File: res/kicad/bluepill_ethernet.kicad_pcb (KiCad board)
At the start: 2 copper layers, 22 parts, among them J1 HEADER-1x20, J2 Conn_01x03, SW1 SW_Push, U1 BluePill_STM32F103C, U2 93C46, U3 WIZ850io

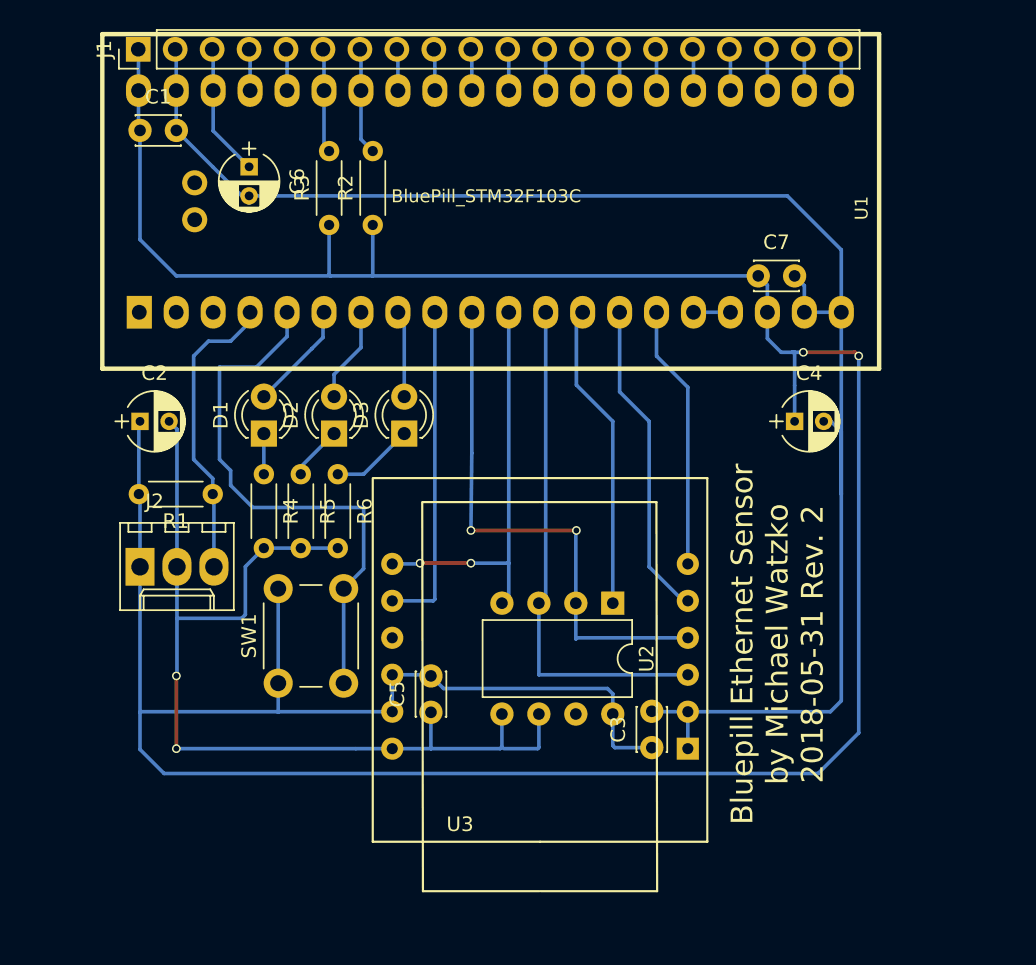
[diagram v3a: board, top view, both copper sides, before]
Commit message: Fix production issues (also add molex pin for other W5500 boards)
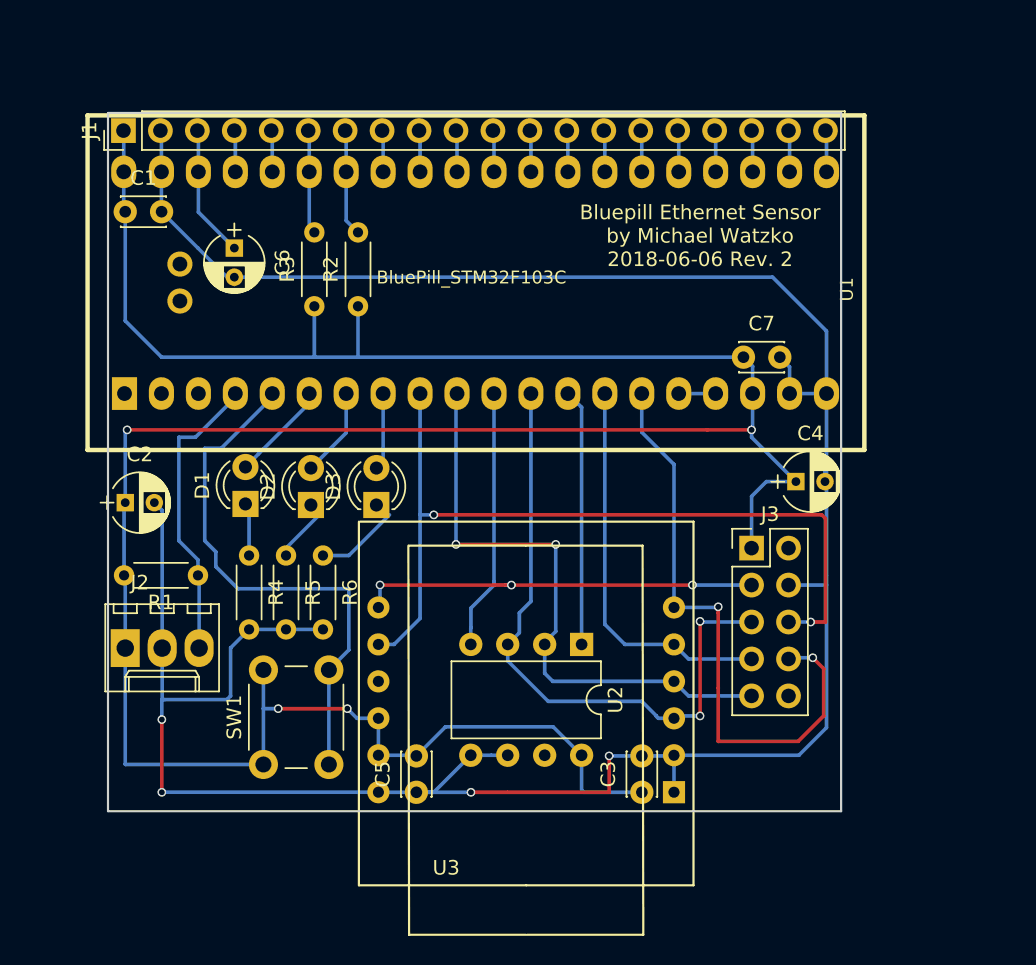
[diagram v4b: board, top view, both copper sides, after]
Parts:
- added J3: Conn_02x05_Odd_Even, Pin_Headers:Pin_Header_Straight_2x05_Pitch2.54mm, F.Cu at (82.0, 61.2)
- moved C7 5.68 mm to (81.5, 48.1)
- moved R4 5.68 mm to (47.5, 61.7)
- moved R5 5.68 mm to (50.0, 61.7)
- moved C1 5.68 mm to (39.0, 38.1)
- moved C2 5.68 mm to (39.0, 58.1)
- moved C6 5.68 mm to (46.5, 40.6)
- moved J1 5.68 mm to (38.9, 32.5)
- moved R1 5.68 mm to (44.0, 63.1)
- moved R2 5.68 mm to (55.0, 44.6)
- moved R3 5.68 mm to (52.0, 44.6)
- moved R6 5.68 mm to (52.6, 61.7)
- moved U1 5.68 mm to (39.0, 50.6)
- moved J2 5.68 mm to (39.0, 68.1)
- moved SW1 5.68 mm to (48.5, 76.1)
- moved C5 5.59 mm to (59.0, 78.0)
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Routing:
- net VCC: track 230.4 -> 195.8 mm, vias 2 -> 4
- net Net-(J3-Pad6): track 22.7 -> 56.7 mm, vias 0 -> 2
- net Net-(J3-Pad8): track 18.2 -> 41.9 mm, vias 0 -> 2
- net Net-(J3-Pad3): track 28.4 -> 46.2 mm, vias 2 -> 3
- net Net-(J3-Pad5): track 35.4 -> 44.0 mm, vias 0 -> 2
- net Net-(J3-Pad7): track 22.0 -> 26.9 mm
- net Net-(J3-Pad9): track 37.5 -> 41.2 mm
- net Net-(U1-Pad13): track 21.2 -> 17.6 mm
- net GND: track 183.1 -> 185.5 mm, vias 2 -> 4
- net Net-(SW1-Pad2): track 38.0 -> 37.2 mm
- net Net-(D3-Pad2): track 5.98 -> 5.31 mm
- net Net-(D1-Pad2): track 7.51 -> 6.87 mm
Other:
- board outline added: 50.4 x 48 mm
- board text added: "Bluepill Ethernet Sensor by Michael Watzko 2018-06-06 Rev. 2"
- board text removed: "Bluepill Ethernet Sensor by Michael Watzko 2018-05-31 Rev. 2"

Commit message: board revision 3 alpha 1
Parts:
- removed C3: C, Capacitors_THT:C_Disc_D3.0mm_W2.0mm_P2.50mm
- added J4: HEADER-1x20, Pin_Headers:Pin_Header_Straight_1x20_Pitch2.54mm, F.Cu at (43.9, 78.2)
- added U4: 93C46, Housings_SSOP:TSSOP-8_4.4x3mm_Pitch0.65mm, F.Cu at (78.9, 41.4)
- C1, C5, C7: footprint Capacitors_THT:C_Disc_D3.0mm_W2.0mm_P2.50mm -> Capacitors_THT:C_Disc_D4.3mm_W1.9mm_P5.00mm
- R1, R2, R3, R4, R5, R6: footprint Resistors_THT:R_Axial_DIN0204_L3.6mm_D1.6mm_P5.08mm_Horizontal -> Resistors_Universal:Resistor_SMD+THTuniversal_0805to1206_RM10_HandSoldering
- moved C2 53.7 mm to (89.7, 40.4), turned to 270 degrees
- moved J2 49.2 mm to (87.4, 59.2), turned to 270 degrees
- moved U2 30.6 mm to (75.2, 37.6), turned to 0 degrees
- moved C5 30.6 mm to (89.1, 72.4), turned to 180 degrees
- moved U3 23.8 mm to (86.6, 65.3), turned to 270 degrees
- moved SW1 20.6 mm to (45.6, 55.7), turned to 0 degrees
- moved R6 14.1 mm to (65.3, 67.7)
- moved R3 12.9 mm to (64.3, 40.6), turned to 180 degrees
- moved R5 12.2 mm to (60.7, 67.7)
- moved C4 12.1 mm to (87.2, 68.6)
- moved R2 11.6 mm to (64.3, 37.6), turned to 180 degrees
- moved R4 10.5 mm to (56.1, 67.7)
- moved J3 9.27 mm to (80.5, 70.4), turned to 180 degrees
- moved R1 9.11 mm to (51.8, 67.7), turned to 90 degrees
- moved D3 9.08 mm to (65.3, 59.2)
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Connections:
- C1 pad 1: VCC -> GND
- C1 pad 2: GND -> VCC
- D1 pad 2: Net-(D1-Pad2) -> (no net)
- D2 pad 2: Net-(D2-Pad2) -> (no net)
- D3 pad 2: Net-(D3-Pad2) -> (no net)
- U1 pad 1: (no net) -> Net-(BT1-Pad1)
- U1 pad 2: (no net) -> Net-(J4-Pad2)
- U1 pad 3: (no net) -> Net-(J4-Pad3)
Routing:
- net Net-(J2-Pad3): track 21.2 -> 96.4 mm, vias 0 -> 1
- net Net-(J4-Pad16): track 2.54 -> 34.8 mm
- net Net-(J4-Pad2): track 0.00 -> 30.4 mm
- net Net-(J4-Pad13): track 17.6 -> 47.9 mm
- net Net-(BT1-Pad1): track 0.00 -> 28.8 mm
- net Net-(J4-Pad3): track 0.00 -> 28.7 mm
- net Net-(D3-Pad2): track 5.31 -> 33.6 mm
- net Net-(J3-Pad9): track 41.2 -> 68.0 mm, vias 2 -> 4
- net Net-(D1-Pad2): track 6.87 -> 33.4 mm
- net VCC: track 195.8 -> 169.5 mm, vias 4 -> 8
- net Net-(J3-Pad5): track 44.0 -> 70.3 mm, vias 2 -> 4
- net Net-(D2-Pad2): track 6.13 -> 31.8 mm
- net Net-(J3-Pad3): track 46.2 -> 67.2 mm, vias 3 -> 4
- net Net-(J3-Pad7): track 26.9 -> 35.4 mm
- net GND: track 185.5 -> 178.9 mm, vias 4 -> 5
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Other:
- board text added: "Bluepill Ethernet Sensor by Michael Watzko 2020-06-15 Rev. 3"
- board text removed: "Bluepill Ethernet Sensor by Michael Watzko 2018-06-06 Rev. 2"

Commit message: Board Rev 3.0
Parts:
- added C3: C, Capacitor_SMD:C_0805_2012Metric, F.Cu at (59.4, 62.3)
- added D10: LED, LED_SMD:LED_1206_3216Metric, F.Cu at (65.9, 73.4)
- added D4: LED, LED_SMD:LED_1206_3216Metric, F.Cu at (65.9, 59.7)
- added D5: LED, LED_SMD:LED_1206_3216Metric, F.Cu at (65.9, 62.0)
- added D6: LED, LED_SMD:LED_1206_3216Metric, F.Cu at (65.9, 64.3)
- added D7: LED, LED_SMD:LED_1206_3216Metric, F.Cu at (65.9, 66.5)
- added D8: LED, LED_SMD:LED_1206_3216Metric, F.Cu at (65.9, 68.8)
- added D9: LED, LED_SMD:LED_1206_3216Metric, F.Cu at (65.9, 71.1)
- added J5: Conn_02x02_Odd_Even, Connector_PinHeader_2.54mm:PinHeader_2x02_P2.54mm_Vertical, F.Cu at (46.7, 58.2)
- added J7: Conn_02x04_Odd_Even, Connector_PinHeader_2.54mm:PinHeader_2x04_P2.54mm_Vertical, F.Cu at (55.4, 62.2)
- added JP1: SolderJumper_2_Bridged, Jumper:SolderJumper-2_P1.3mm_Bridged_RoundedPad1.0x1.5mm, F.Cu at (66.8, 39.5)
- added JP2: SolderJumper_2_Bridged, Jumper:SolderJumper-2_P1.3mm_Bridged_RoundedPad1.0x1.5mm, F.Cu at (54.1, 39.7)
- added JP3: SolderJumper_2_Bridged, Jumper:SolderJumper-2_P1.3mm_Bridged_RoundedPad1.0x1.5mm, F.Cu at (71.9, 39.5)
- added JP4: SolderJumper_2_Bridged, Jumper:SolderJumper-2_P1.3mm_Bridged_RoundedPad1.0x1.5mm, F.Cu at (69.3, 39.5)
- added JP5: SolderJumper_2_Bridged, Jumper:SolderJumper-2_P1.3mm_Bridged_RoundedPad1.0x1.5mm, F.Cu at (64.3, 39.5)
- added JP6: SolderJumper_2_Bridged, Jumper:SolderJumper-2_P1.3mm_Bridged_RoundedPad1.0x1.5mm, F.Cu at (61.7, 39.5)
- added JP7: SolderJumper_2_Bridged, Jumper:SolderJumper-2_P1.3mm_Bridged_RoundedPad1.0x1.5mm, F.Cu at (59.2, 36.1)
- added JP8: SolderJumper_2_Bridged, Jumper:SolderJumper-2_P1.3mm_Bridged_RoundedPad1.0x1.5mm, F.Cu at (56.6, 36.1)
- added R7: R, Resistor_SMD:R_0805_2012Metric, F.Cu at (69.9, 70.6)
- added R8: R, Resistor_SMD:R_0805_2012Metric, F.Cu at (69.9, 72.6)
- added RN2: 4,7k, Resistor_THT:R_Array_SIP9, F.Cu at (51.6, 37.8)
- added U5: PCF8574A, Package_SO:TSSOP-20_4.4x6.5mm_P0.65mm, F.Cu at (58.4, 71.4)
- added U6: LM75B, Package_SO:VSSOP-8_3.0x3.0mm_P0.65mm, F.Cu at (88.3, 38.4)
- D1, D2: footprint LEDs:LED_D3.0mm -> LED_THT:LED_D3.0mm
- D3: footprint LEDs:LED_D3.0mm -> LED_SMD:LED_1206_3216Metric
- R1, R2, R3, R4, R5, R6: footprint Resistors_Universal:Resistor_SMD+THTuniversal_0805to1206_RM10_HandSoldering -> Resistor_SMD:R_0805_2012Metric
- moved R2 23.6 mm to (69.9, 60.5)
- moved R3 22.6 mm to (69.9, 62.5)
- moved R1 20.4 mm to (69.9, 58.4), turned to 180 degrees
- moved SW1 14.5 mm to (45.5, 70.2)
- moved R4 14.2 mm to (69.9, 64.5), turned to 180 degrees
- moved R5 9.30 mm to (69.9, 66.5), turned to 180 degrees
- moved C1 6.12 mm to (49.3, 42.7), turned to 180 degrees
- moved R6 4.73 mm to (69.9, 68.6), turned to 180 degrees
- moved D1 2.32 mm to (53.8, 58.8)
- moved C2 2.29 mm to (89.7, 42.7), turned to 0 degrees
- moved D3 1.89 mm to (65.9, 57.4), turned to 0 degrees
- moved C6 1.80 mm to (48.3, 38.6), turned to 180 degrees
- moved J4 1.78 mm to (43.9, 80.0)
- moved J1 0.76 mm to (43.9, 31.8)
- moved D2 0.57 mm to (60.2, 58.9)
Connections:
- D1 pad 2: (no net) -> dled1
- D2 pad 2: (no net) -> dled2
- D3 pad 2: (no net) -> Net-(D3-Pad2)
- J4 pad 15: Net-(J3-Pad8) -> i2c1c
- J4 pad 16: Net-(J4-Pad16) -> i2c1d
- J4 pad 17: Net-(J4-Pad16) -> Net-(J4-Pad17)
- J4 pad 4: Net-(J2-Pad3) -> Net-(J4-Pad4)
- J4 pad 6: Net-(D1-Pad2) -> Net-(J3-Pad8)
- J4 pad 7: Net-(D2-Pad2) -> Net-(J4-Pad17)
- J4 pad 8: Net-(D3-Pad2) -> Net-(J2-Pad3)
- R1 pad 1: Net-(J2-Pad3) -> VCC
- R1 pad 2: VCC -> Net-(D3-Pad2)
- R2 pad 2: Net-(J1-Pad7) -> Net-(D4-Pad2)
- R3 pad 2: Net-(J1-Pad6) -> Net-(D5-Pad2)
- R4 pad 1: Net-(D1-Pad1) -> VCC
- R4 pad 2: GND -> Net-(D6-Pad2)
- R5 pad 1: Net-(D2-Pad1) -> VCC
- R5 pad 2: GND -> Net-(D7-Pad2)
- R6 pad 1: Net-(D3-Pad1) -> VCC
- R6 pad 2: GND -> Net-(D8-Pad2)
- U1 pad 15: Net-(J3-Pad8) -> i2c1c
- U1 pad 16: Net-(J4-Pad16) -> i2c1d
- U1 pad 17: Net-(J4-Pad16) -> Net-(J4-Pad17)
- U1 pad 3: Net-(J4-Pad3) -> Net-(J5-Pad2)
- U1 pad 4: Net-(J2-Pad3) -> Net-(J5-Pad4)
- U1 pad 6: Net-(D1-Pad2) -> Net-(J3-Pad8)
- U1 pad 7: Net-(D2-Pad2) -> Net-(J4-Pad17)
- U1 pad 8: Net-(D3-Pad2) -> Net-(J2-Pad3)
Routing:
- net i2c1c: track 0.00 -> 127.5 mm, vias 0 -> 7
- net i2c1d: track 0.00 -> 122.7 mm, vias 0 -> 5
- net Net-(J4-Pad17): track 0.00 -> 105.7 mm, vias 0 -> 2
- net VCC: track 169.5 -> 233.3 mm, vias 8 -> 4
- net GND: track 178.9 -> 219.5 mm, vias 5 -> 9
- net Net-(J4-Pad16): track 34.8 -> 0.00 mm
- net Net-(D1-Pad2): track 33.4 -> 0.00 mm
- net Net-(J4-Pad4): track 0.00 -> 32.2 mm
- net Net-(D2-Pad2): track 31.8 -> 0.00 mm
- net Net-(D3-Pad2): track 33.6 -> 2.10 mm
- net Net-(D4-Pad1): track 0.00 -> 29.2 mm, vias 0 -> 2
- net Net-(J3-Pad8): track 44.3 -> 64.8 mm, vias 6 -> 1
- net dled2: track 0.00 -> 19.8 mm
- net dled1: track 0.00 -> 19.4 mm, vias 0 -> 1
- net Net-(D5-Pad1): track 0.00 -> 17.4 mm
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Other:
- board size 50.4 x 48 mm -> 50.4 x 50.4 mm
- board text added: "Bluepill Ethernet Sensor by Michael Watzko 2020-06-17 Rev 3.0"
- board text added: "EEPROM 93c46"
- board text added: "GND"
- board text added: "I2C GPIO PCF8574"
- board text added: "LED1"
- board text added: "LED2"
- board text added: "P0"
- board text added: "P1"
- board text added: "P2"
- board text added: "P3"
- board text added: "P4"
- board text added: "P5"
- board text added: "P6"
- board text added: "P7"
- board text added: "PA0"
- board text added: "PA3"
- board text added: "PB10"
- board text added: "PB11"
- board text added: "PC14"
- board text added: "PC15"
- board text added: "Temp LM75"
- board text added: "VCC"
- board text removed: "Bluepill Ethernet Sensor by Michael Watzko 2020-06-15 Rev. 3"

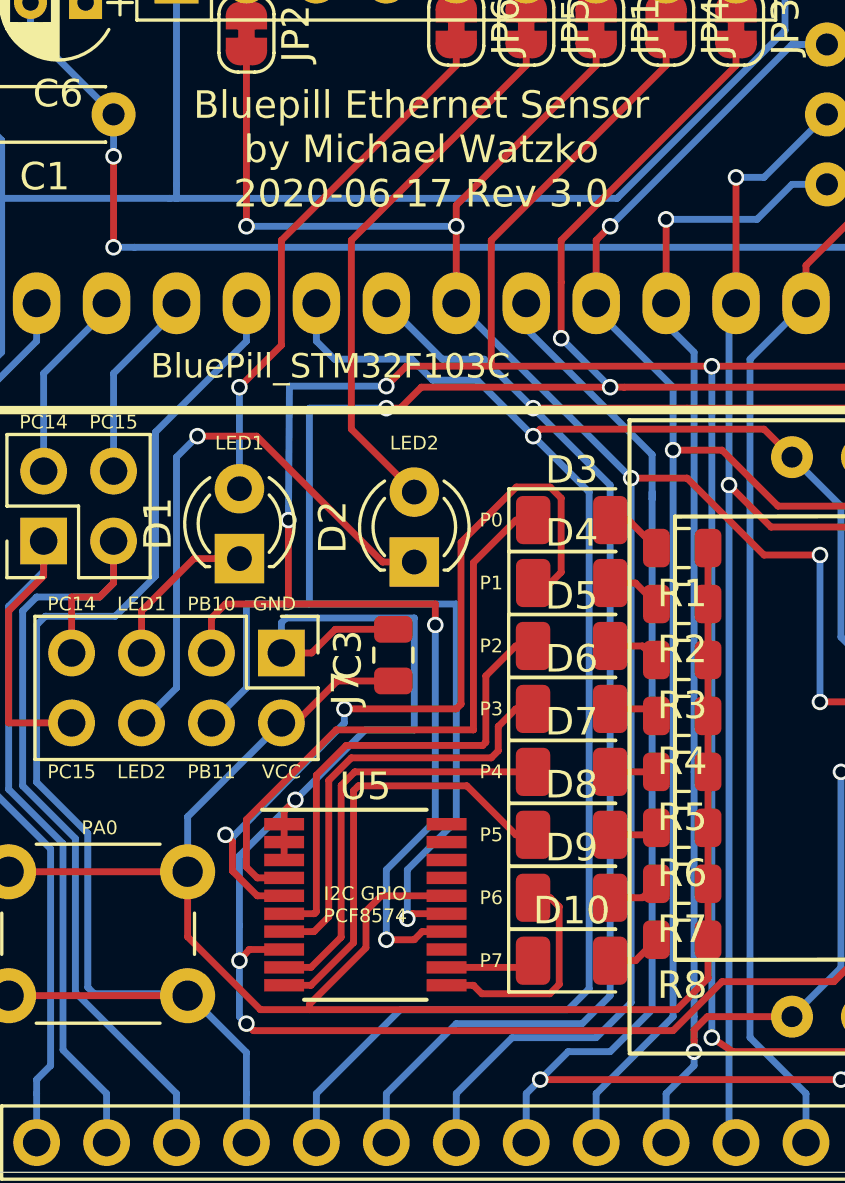
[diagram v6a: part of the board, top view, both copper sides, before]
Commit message: Board rev 3.1: Fix invalid pcf8574 footprint (20->16 pins)
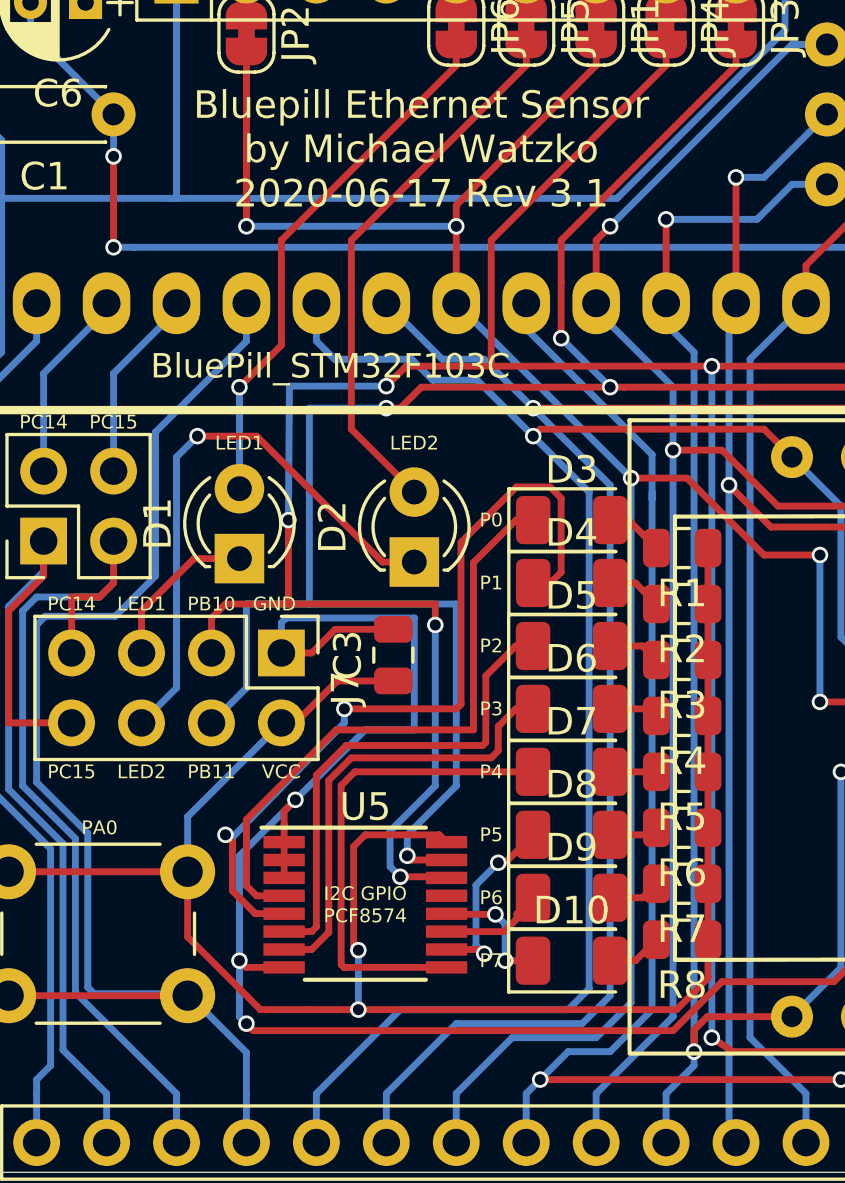
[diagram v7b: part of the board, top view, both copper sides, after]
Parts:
- U5: footprint Package_SO:TSSOP-20_4.4x6.5mm_P0.65mm -> Package_SO:TSSOP-16_4.4x5mm_P0.65mm
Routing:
- net Net-(D8-Pad1): track 16.0 -> 6.91 mm, vias 0 -> 2
- net Net-(D9-Pad1): track 8.27 -> 3.75 mm
- net i2c1c: track 127.5 -> 124.7 mm
- net VCC: track 233.3 -> 235.8 mm, vias 4 -> 6
- net Net-(D7-Pad1): track 15.2 -> 17.6 mm
- net i2c1d: track 122.7 -> 120.4 mm
- net Net-(D10-Pad1): track 3.24 -> 4.62 mm, vias 0 -> 2
- net Net-(D4-Pad1): track 29.2 -> 29.9 mm
- net Net-(D3-Pad1): track 21.7 -> 22.4 mm
- net Net-(D6-Pad1): track 15.8 -> 16.4 mm
- net Net-(D5-Pad1): track 17.4 -> 18.0 mm
- net GND: track 219.5 -> 220.0 mm
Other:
- board text added: "Bluepill Ethernet Sensor by Michael Watzko 2020-06-17 Rev 3.1"
- board text removed: "Bluepill Ethernet Sensor by Michael Watzko 2020-06-17 Rev 3.0"
